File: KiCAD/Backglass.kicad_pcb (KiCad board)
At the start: 2 copper layers, 48.3 x 40.6 mm, 55 parts, among them J1 IO Header, J11 Header_ICSP_AVR, J12 Header_ICSP_AVR, J13 Header_ICSP_AVR, J2 RAMP Header, J3 OUT Header, J4 Micro_USB_Connector, J5 Batteries, Q1 MOSFET_N_E, Q2 MOSFET_N_E+P_E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

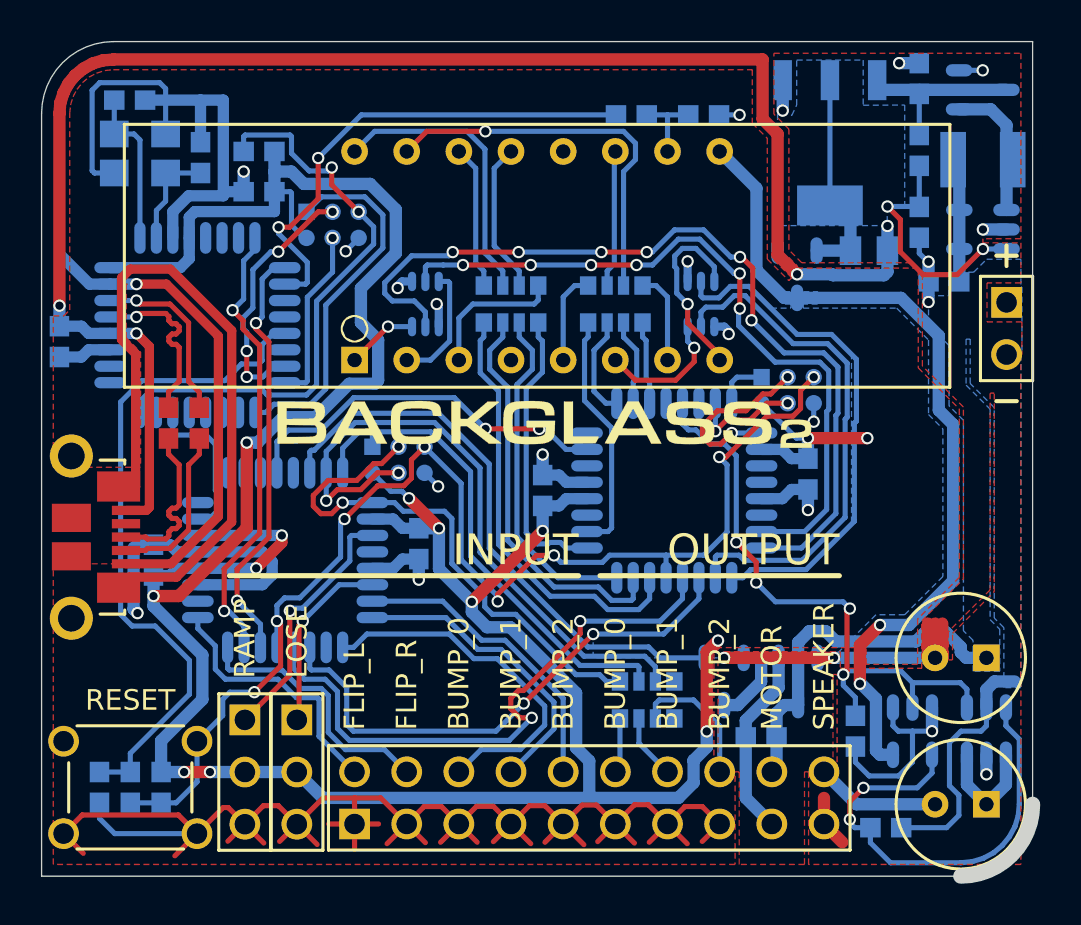
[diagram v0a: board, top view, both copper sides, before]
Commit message: Fixed audio output, reduced power consumption
Removed half-bridge and associated components, modified resistor values
to drive LEDs dimmer (and now within power specs for the 48PB).
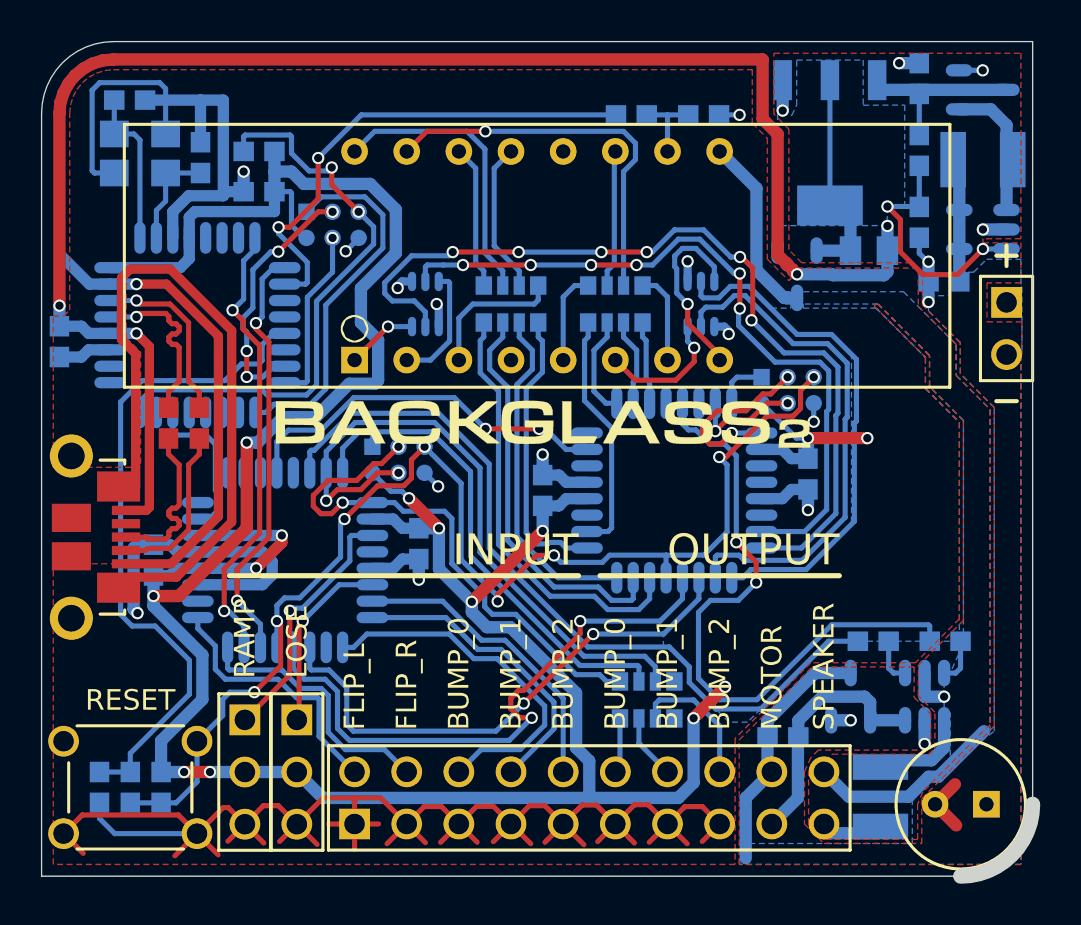
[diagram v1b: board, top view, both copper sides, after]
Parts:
- removed C4: 220u, M_Through-hole:C_6.3-2.5mm
- removed the Q2 at (162.8, 104.7)
- removed the U4 at (159.2, 104.7)
- added R10: 10, M_SMD:3225, B.Cu at (157.7, 107.9)
- J3: value OUT Header -> LOSE Header
- Q1: value MOSFET_N_E -> MOSFET_N_E_Dual; footprint M_SMD:SOT-23-3_GSD -> M_SMD:SOT-23-6_G1-S2-G2-D2-S1-D1
- R4: value 180 -> 1K
- R7: value 1K -> 5.6K
- R8, R9: value 10K -> 1K
- RN1, RN2, RN3: value 150 -> 270
- U1: value ATmega16U2-AU -> ATmega8U2-AU
- moved Q1 9.79 mm to (159.8, 103.0)
- moved R8 9.10 mm to (157.3, 100.3)
- moved C13 7.13 mm to (161.6, 108.3)
- moved R9 6.19 mm to (160.8, 100.3), turned to 180 degrees
- moved D1 2.66 mm to (156.2, 103.0), turned to 180 degrees
- moved C3 1.06 mm to (152.9, 105.0), turned to 180 degrees
- moved G*** 0.08 mm to (141.3, 89.8)
- renumbered Q3 to Q2, Q4 to Q3, R10 to R11, R11 to R12, U5 to U4, U6 to U5
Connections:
- net OUT_SENSE renamed LOSE_SENSE
- J1 pad 19: GND -> SPEAKER-
- J1 pad 20: SPEAKER -> +5V
- R8 pad 1: +V_BATT -> Net-(Q1-PadG1)
- R8 pad 2: Net-(Q2-PadG2) (its old number) -> MOTOR_SIG
- R9 pad 1: AUDIO_SIG -> Net-(Q1-PadG2)
- R9 pad 2: GND -> AUDIO_SIG
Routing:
- net +5V: track 190.9 -> 166.2 mm, vias 16 -> 14
- net GND: track 252.7 -> 230.0 mm, vias 27 -> 26
- net Net-(Q2-PadG2) (its old number): track 22.6 -> 0.00 mm, vias 2 -> 0
- net +V_BATT: track 36.5 -> 18.6 mm
- net MOTOR_SIG: track 28.4 -> 38.7 mm
- net SPEAKER: track 6.06 -> 0.00 mm
- net Net-(C4-Pad1): track 5.61 -> 0.00 mm
- net Net-(Q1-PadD2): track 0.00 -> 4.83 mm
- net SPEAKER-: track 0.00 -> 3.33 mm
- net Net-(Q1-PadG2): track 0.00 -> 2.21 mm
- net Net-(Q1-PadG1): track 0.00 -> 2.21 mm
- net MOTOR-: track 13.6 -> 12.6 mm
- net AUDIO_SIG: track 30.9 -> 31.4 mm, vias 4 -> 2
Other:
- board text added: "git.io/v9lfx"
- board text added: "rev2"
